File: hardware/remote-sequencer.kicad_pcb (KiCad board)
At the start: 2 copper layers, 90 x 65 mm, 24 parts, among them J1 PWR_IN, J2 RF_SENSE_BOARD, J3 RELAY_LED_OUT, J4 RELAY_OUT, J5 RF_SENSE_DISABLE, J6 DTMF_MODULE, J7 ON, J8 OFF, U1 LM7805_TO220

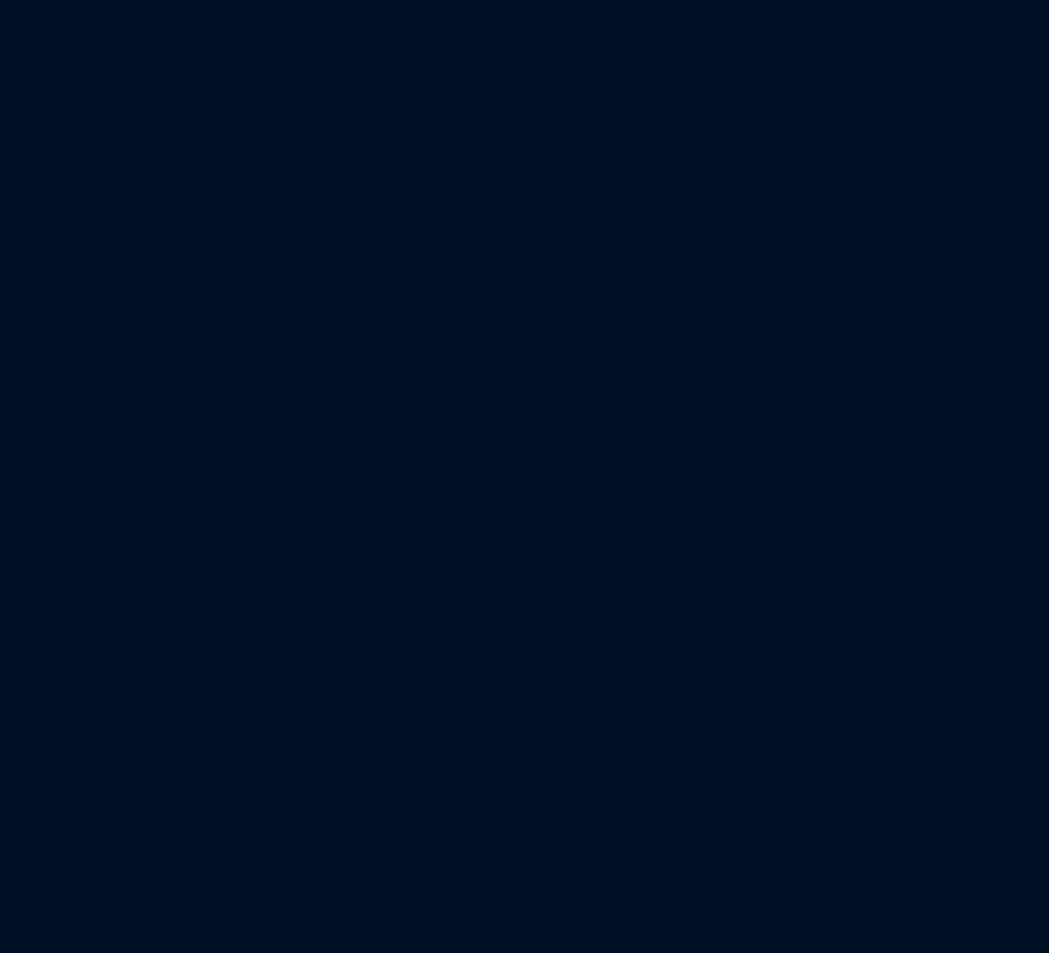
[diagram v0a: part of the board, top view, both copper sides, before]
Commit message: adds relay board schematic and pcb
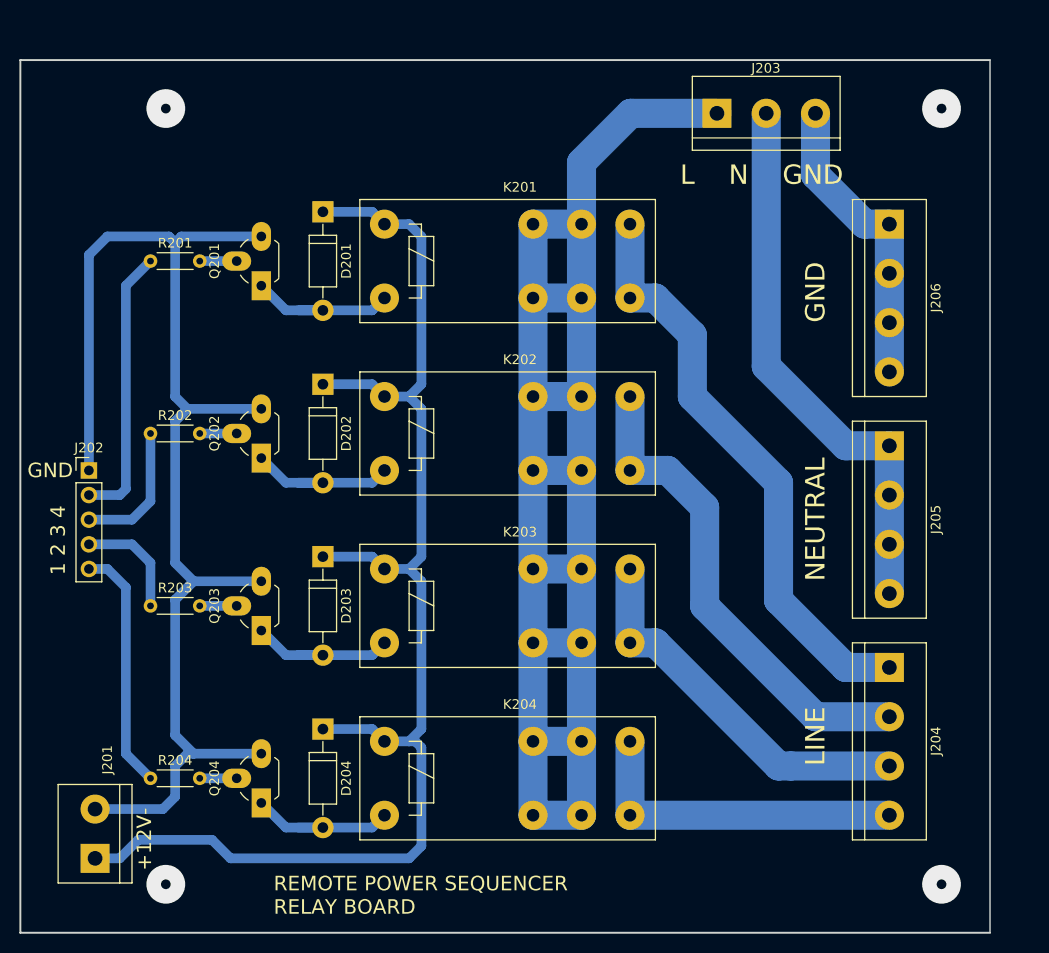
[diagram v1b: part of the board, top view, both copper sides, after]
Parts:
- added D201: 1N4148, Diodes_ThroughHole:D_DO-41_SOD81_P10.16mm_Horizontal, F.Cu at (76.2, 120.7)
- added D202: 1N4148, Diodes_ThroughHole:D_DO-41_SOD81_P10.16mm_Horizontal, F.Cu at (76.2, 138.4)
- added D203: 1N4148, Diodes_ThroughHole:D_DO-41_SOD81_P10.16mm_Horizontal, F.Cu at (76.2, 156.2)
- added D204: 1N4148, Diodes_ThroughHole:D_DO-41_SOD81_P10.16mm_Horizontal, F.Cu at (76.2, 174.0)
- added J201: PWR_IN, Terminal_Blocks:TerminalBlock_bornier-2_P5.08mm, F.Cu at (52.7, 187.3)
- added J202: RELAY_IN, Socket_Strips:Socket_Strip_Straight_1x05_Pitch2.54mm, F.Cu at (52.1, 147.3)
- added J203: AC_POWER_IN, Terminal_Blocks:TerminalBlock_bornier-3_P5.08mm, F.Cu at (116.8, 110.5)
- added J204: PWR_OUT, Terminal_Blocks:TerminalBlock_bornier-4_P5.08mm, F.Cu at (134.6, 167.6)
- added J205: NEUTRAL_OUT, Terminal_Blocks:TerminalBlock_bornier-4_P5.08mm, F.Cu at (134.6, 144.8)
- added J206: EARTH_OUT, Terminal_Blocks:TerminalBlock_bornier-4_P5.08mm, F.Cu at (134.6, 121.9)
- added K201: RELAY_DPDT, Relays_ThroughHole:Relay_SPDT_Schrack-RP-II-1-16A-FormC_RM5mm, F.Cu at (82.5, 121.9)
- added K202: RELAY_DPDT, Relays_ThroughHole:Relay_SPDT_Schrack-RP-II-1-16A-FormC_RM5mm, F.Cu at (82.5, 139.7)
- added K203: RELAY_DPDT, Relays_ThroughHole:Relay_SPDT_Schrack-RP-II-1-16A-FormC_RM5mm, F.Cu at (82.5, 157.5)
- added K204: RELAY_DPDT, Relays_ThroughHole:Relay_SPDT_Schrack-RP-II-1-16A-FormC_RM5mm, F.Cu at (82.5, 175.3)
- added Q201: BC548, TO_SOT_Packages_THT:TO-92_Rugged, F.Cu at (69.8, 128.3)
- added Q202: BC548, TO_SOT_Packages_THT:TO-92_Rugged, F.Cu at (69.8, 146.1)
- added Q203: BC548, TO_SOT_Packages_THT:TO-92_Rugged, F.Cu at (69.8, 163.8)
- added Q204: BC548, TO_SOT_Packages_THT:TO-92_Rugged, F.Cu at (69.8, 181.6)
- added R201: 1k, Resistors_ThroughHole:R_Axial_DIN0204_L3.6mm_D1.6mm_P5.08mm_Horizontal, F.Cu at (58.4, 125.7)
- added R202: 1k, Resistors_ThroughHole:R_Axial_DIN0204_L3.6mm_D1.6mm_P5.08mm_Horizontal, F.Cu at (58.4, 143.5)
- added R203: 1k, Resistors_ThroughHole:R_Axial_DIN0204_L3.6mm_D1.6mm_P5.08mm_Horizontal, F.Cu at (58.4, 161.3)
- added R204: 1k, Resistors_ThroughHole:R_Axial_DIN0204_L3.6mm_D1.6mm_P5.08mm_Horizontal, F.Cu at (58.4, 179.1)
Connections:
- A1 pad 1: (no net) -> Net-(A1-Pad1)
- A1 pad 11: (no net) -> Net-(A1-Pad11)
- A1 pad 16: (no net) -> Net-(A1-Pad16)
- A1 pad 17: (no net) -> Net-(A1-Pad17)
- A1 pad 18: (no net) -> Net-(A1-Pad18)
- A1 pad 2: (no net) -> Net-(A1-Pad2)
- A1 pad 22: (no net) -> Net-(A1-Pad22)
- A1 pad 23: (no net) -> Net-(A1-Pad23)
- A1 pad 24: (no net) -> Net-(A1-Pad24)
- A1 pad 25: (no net) -> Net-(A1-Pad25)
- A1 pad 26: (no net) -> Net-(A1-Pad26)
- A1 pad 27: (no net) -> Net-(A1-Pad27)
- A1 pad 28: (no net) -> Net-(A1-Pad28)
- A1 pad 3: (no net) -> Net-(A1-Pad3)
- J6 pad 6: (no net) -> Net-(J6-Pad6)
- J6 pad 7: (no net) -> Net-(J6-Pad7)
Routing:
- net LINE: track 0.00 -> 184.3 mm
- net +12V: track 10.2 -> 151.8 mm
- net GND: track 300.2 -> 433.6 mm
- net /RelayBoard/PWR_OUT_1: track 0.00 -> 61.0 mm
- net NEUT: track 0.00 -> 57.4 mm
- net /RelayBoard/PWR_OUT_2: track 0.00 -> 50.8 mm
- net /RelayBoard/PWR_OUT_3: track 0.00 -> 39.6 mm
- net /RelayBoard/PWR_OUT_4: track 0.00 -> 34.4 mm
- net Earth_Protective: track 0.00 -> 31.3 mm
- net /RelayBoard/CTRL_1: track 0.00 -> 28.6 mm
- net /RelayBoard/CTRL_4: track 0.00 -> 25.3 mm
- net Net-(D204-Pad2): track 0.00 -> 16.8 mm
- net Net-(D203-Pad2): track 0.00 -> 16.8 mm
- net Net-(D202-Pad2): track 0.00 -> 16.8 mm
- net Net-(D201-Pad2): track 0.00 -> 16.8 mm
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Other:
- board size 90 x 65 mm -> 210 x 125 mm
- board text added: "1 2 3 4"
- board text added: "L N GND"
- board text added: "LINE"
- board text added: "NEUTRAL"
- board text added: "REMOTE POWER SEQUENCER RELAY BOARD"

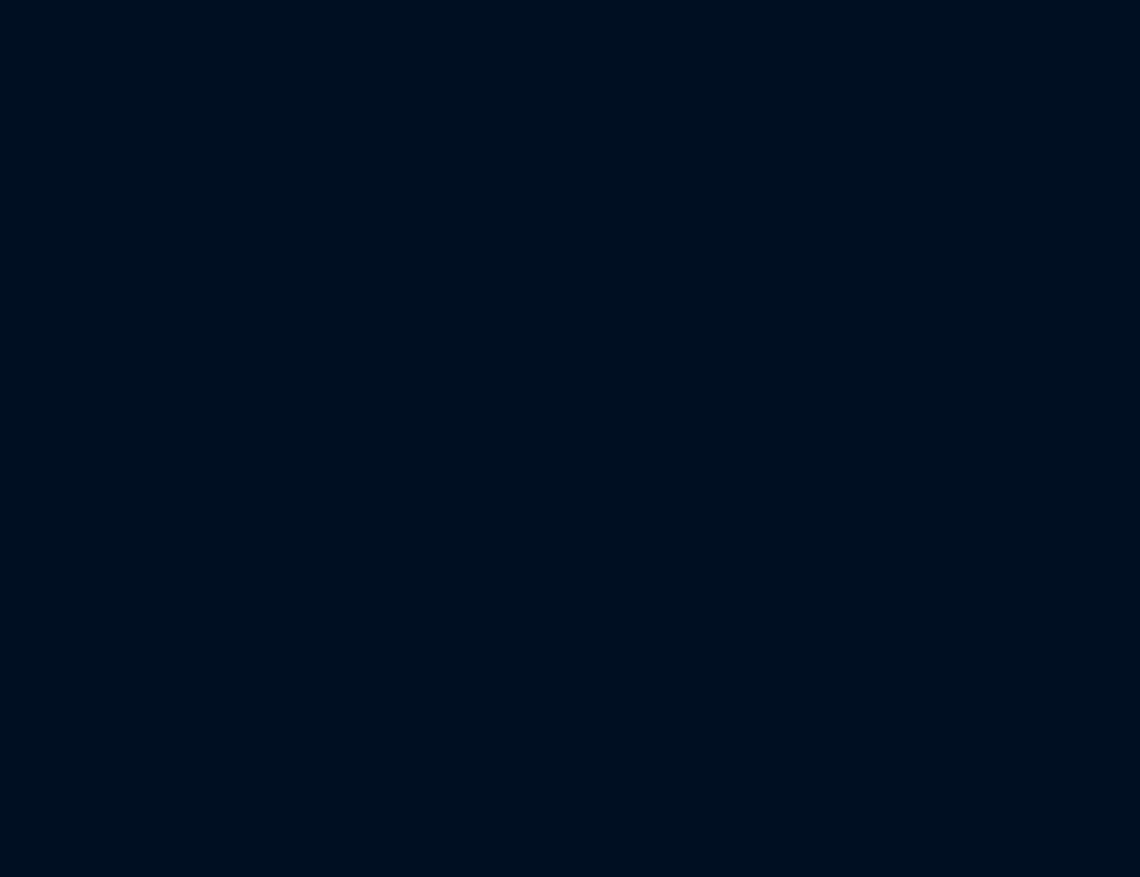
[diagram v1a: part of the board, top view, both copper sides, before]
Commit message: adds rf sense board schematic and pcb
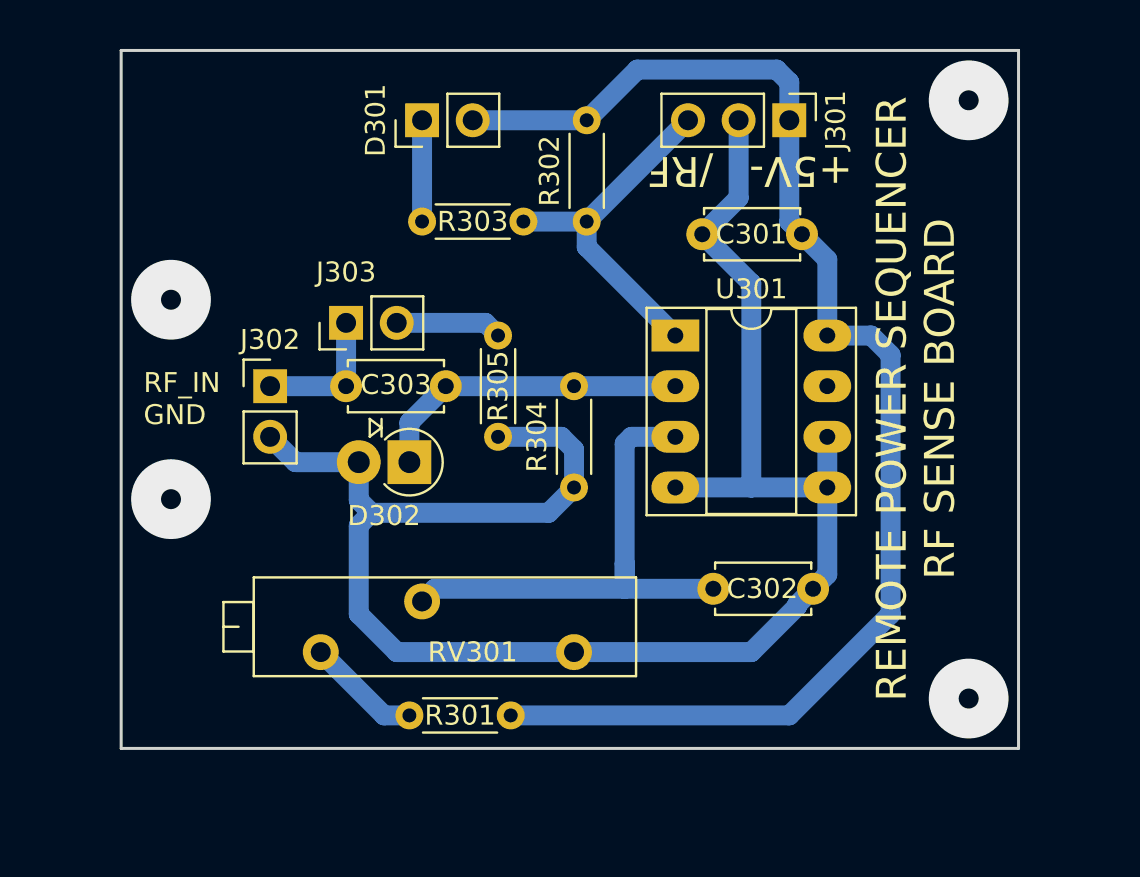
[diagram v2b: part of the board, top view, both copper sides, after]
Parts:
- added C301: 100n, Capacitors_ThroughHole:C_Disc_D4.7mm_W2.5mm_P5.00mm, F.Cu at (104.1, 69.2)
- added C302: 100n, Capacitors_ThroughHole:C_Disc_D4.7mm_W2.5mm_P5.00mm, F.Cu at (99.7, 87.0)
- added C303: 100n, Capacitors_ThroughHole:C_Disc_D4.7mm_W2.5mm_P5.00mm, F.Cu at (86.3, 76.8)
- added D301: RF OK, Socket_Strips:Socket_Strip_Straight_1x02_Pitch2.54mm, F.Cu at (85.1, 63.5)
- added D302: 1N4148, Diodes_ThroughHole:D_DO-41_SOD81_P2.54mm_Vertical_AnodeUp, F.Cu at (84.5, 80.6)
- added J301: RF_SENSE_BOARD, Pin_Headers:Pin_Header_Straight_1x03_Pitch2.54mm, F.Cu at (103.5, 63.5)
- added J302: RF_PROBE_IN, Socket_Strips:Socket_Strip_Straight_1x02_Pitch2.54mm, F.Cu at (77.5, 76.8)
- added J303: 51_ENABLE, Socket_Strips:Socket_Strip_Straight_1x02_Pitch2.54mm, F.Cu at (81.3, 73.7)
- added R301: 10k, Resistors_ThroughHole:R_Axial_DIN0204_L3.6mm_D1.6mm_P5.08mm_Horizontal, F.Cu at (84.5, 93.3)
- added R302: 1k, Resistors_ThroughHole:R_Axial_DIN0204_L3.6mm_D1.6mm_P5.08mm_Horizontal, F.Cu at (93.3, 68.6)
- added R303: 1k, Resistors_ThroughHole:R_Axial_DIN0204_L3.6mm_D1.6mm_P5.08mm_Horizontal, F.Cu at (90.2, 68.6)
- added R304: 100K, Resistors_ThroughHole:R_Axial_DIN0204_L3.6mm_D1.6mm_P5.08mm_Horizontal, F.Cu at (92.7, 81.9)
- added R305: 51, Resistors_ThroughHole:R_Axial_DIN0204_L3.6mm_D1.6mm_P5.08mm_Horizontal, F.Cu at (88.9, 79.4)
- added RV301: 1k, Potentiometers:Potentiometer_Trimmer_Bourns_3006P, F.Cu at (92.7, 90.2)
- added U301: LM393, Housings_DIP:DIP-8_W7.62mm_Socket_LongPads, F.Cu at (97.8, 74.3)
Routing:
- net GND: track 433.6 -> 524.1 mm
- net +5V: track 111.6 -> 180.0 mm
- net Net-(C302-Pad1): track 0.00 -> 25.5 mm
- net Net-(J301-Pad3): track 0.00 -> 17.9 mm
- net Net-(C303-Pad1): track 0.00 -> 16.1 mm
- net Net-(C303-Pad2): track 0.00 -> 6.98 mm
- net Net-(R301-Pad1): track 0.00 -> 5.76 mm
- net Net-(J303-Pad2): track 0.00 -> 5.34 mm
- net Net-(D301-Pad1): track 0.00 -> 5.08 mm
- net (no net): vias 8 -> 12
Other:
- board size 210 x 125 mm -> 210 x 135 mm
- board text added: "+5V-"
- board text added: "/RF"
- board text added: "REMOTE POWER SEQUENCER RF SENSE BOARD"
- board text added: "RF_IN GND"
